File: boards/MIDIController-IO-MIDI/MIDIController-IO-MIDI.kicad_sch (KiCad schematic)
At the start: 44 parts, among them J1 MIDI In 1, J10 MIDICon, J2 MIDI In 2, J3 MIDI In 3, J4 MIDI In 4, J5 MIDI In Pedal, J6 MIDI Out 1, J7 MIDI Out 2, J8 MIDI Out 3, J9 MIDI Out 4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

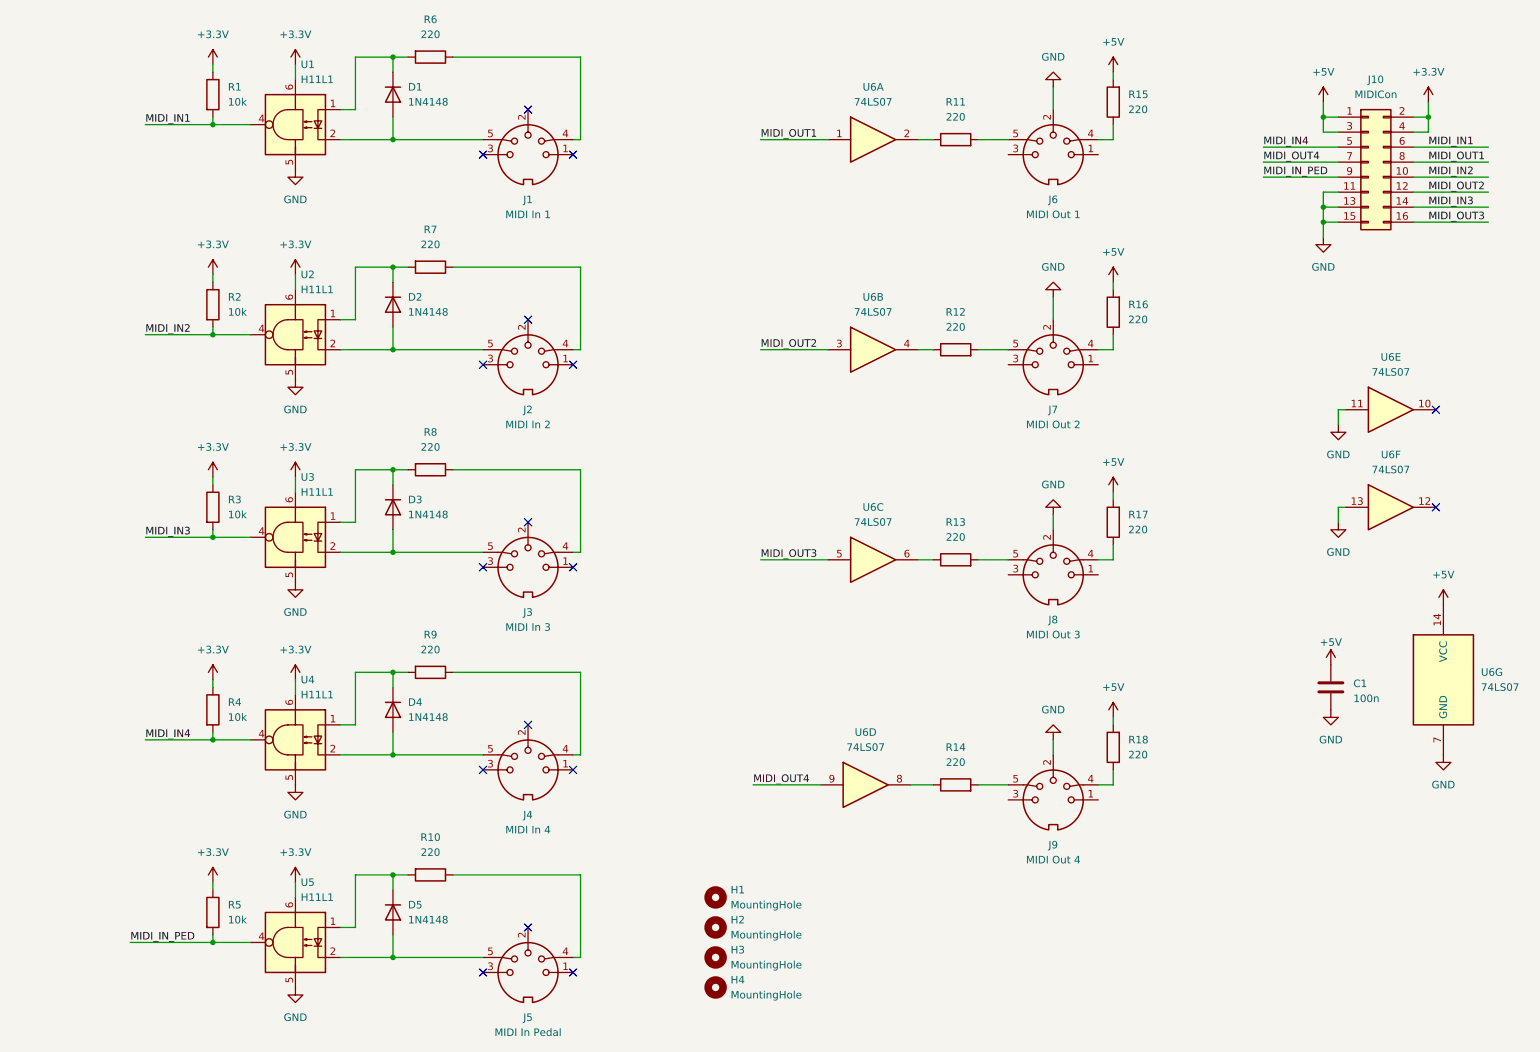
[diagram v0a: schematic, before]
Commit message: Finished PCB for MIDI IO board
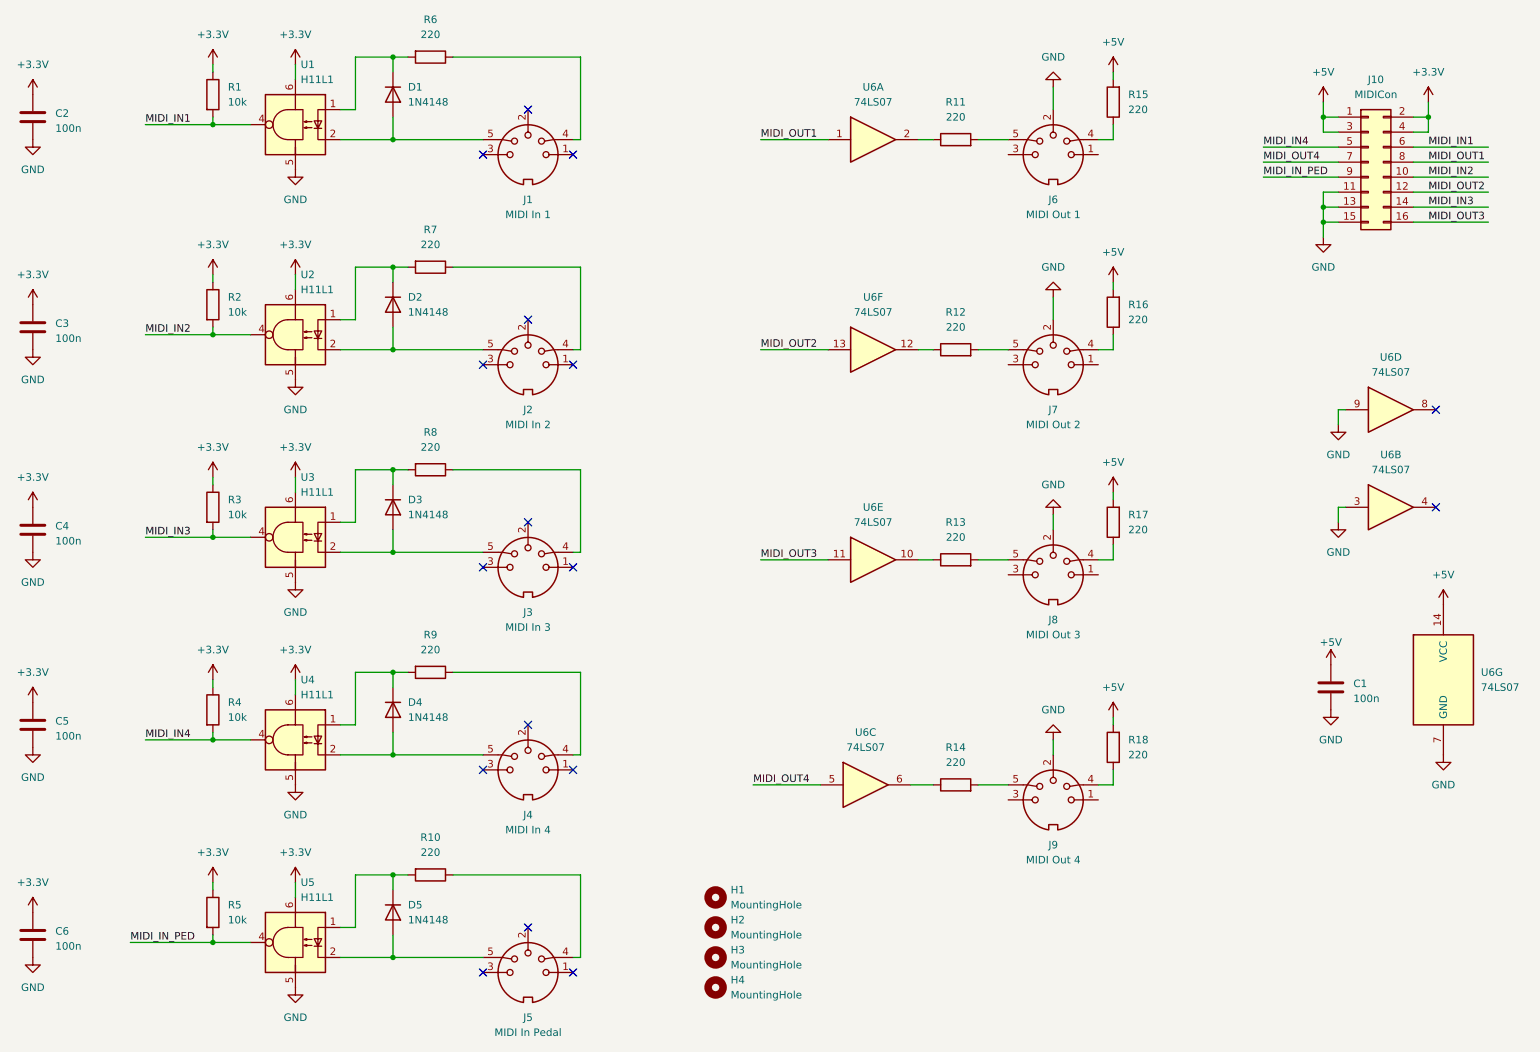
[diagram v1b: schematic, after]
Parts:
- added C2, C3, C4, C5, C6: 100n, Capacitor_THT:C_Disc_D5.0mm_W2.5mm_P5.00mm, symbol Device:C
- R1, R10, R11, R12, R13, R14, R15, R16, R17, R18, R2, R3, R4, R5, R6, R7, R8, R9: footprint Resistor_THT:R_Axial_DIN0204_L3.6mm_D1.6mm_P2.54mm_Vertical -> Resistor_THT:R_Axial_DIN0204_L3.6mm_D1.6mm_P7.62mm_Horizontal
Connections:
- net +3.3V: now also C2.1, C3.1, C4.1, C5.1, C6.1
- net GND: now also U6.3, U6.9, C2.2, C3.2, C4.2, C5.2, C6.2; no longer U6.11, U6.13
- net MIDI_OUT2: now also U6.13; no longer U6.3
- net MIDI_OUT3: now also U6.11; no longer U6.5
- net MIDI_OUT4: now also U6.5; no longer U6.9
- net at R14.1: now also U6.6; no longer U6.8
- net at U6.12: now also R12.1
- net at R13.1: now also U6.10; no longer U6.6
- net at U6.4: no longer R12.1
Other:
- moved on the sheet: U6B, U6C, U6D, U6E, U6F

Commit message: Added Optocoupler and RS232 converter to UART board lines.
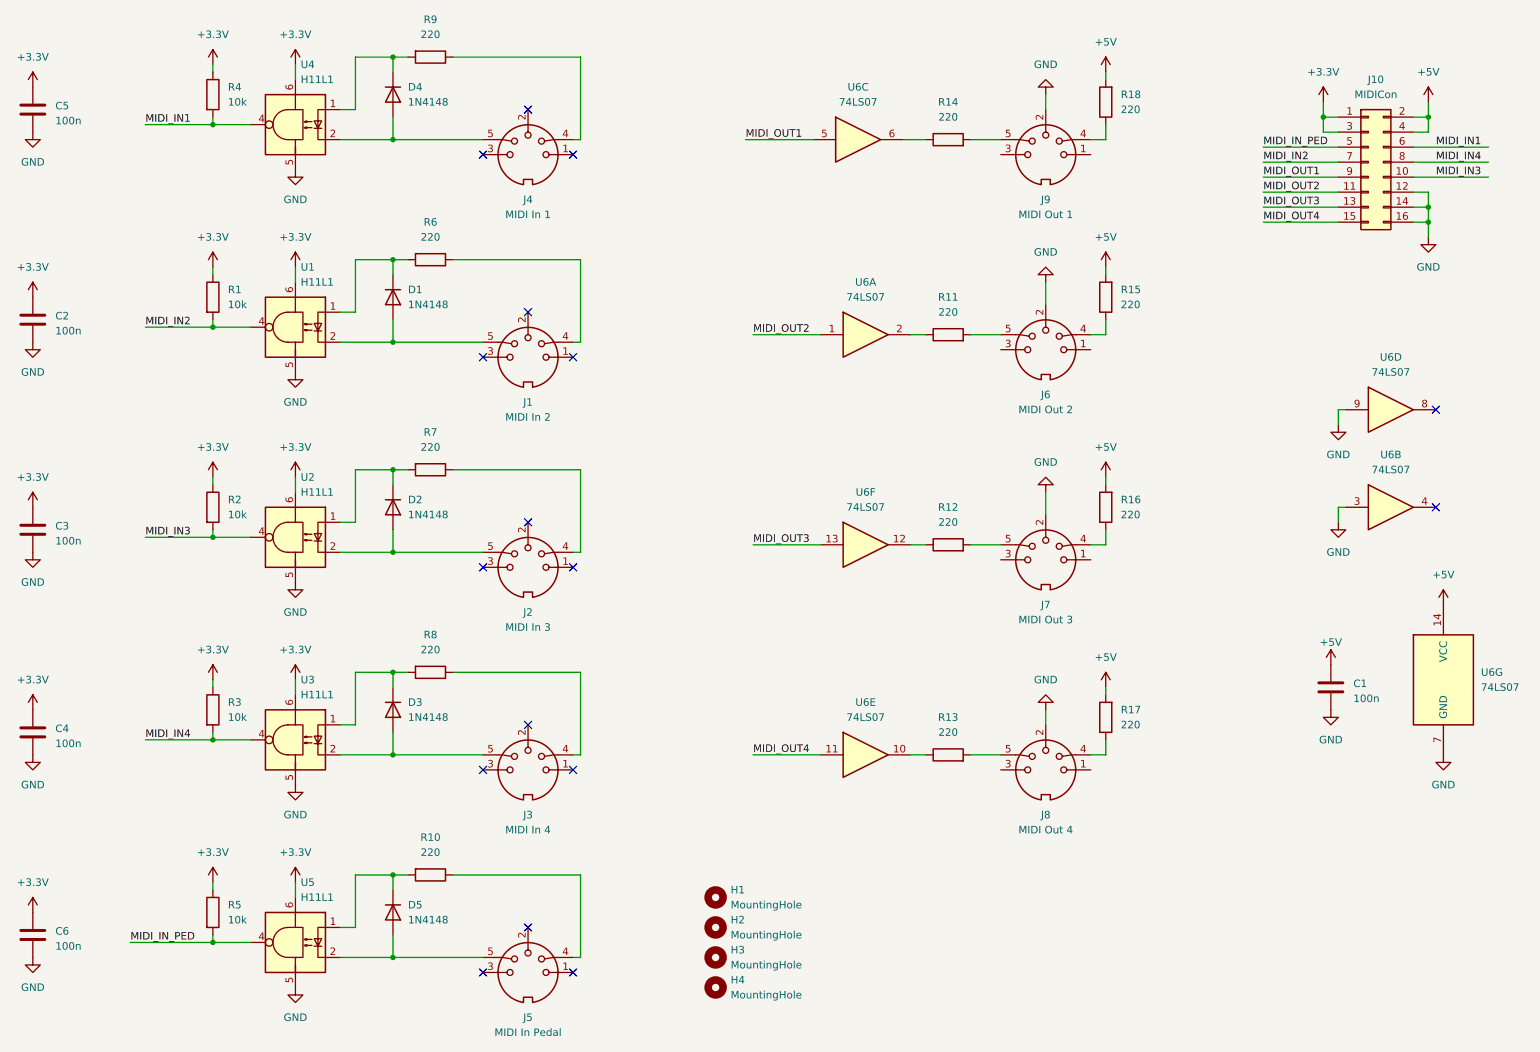
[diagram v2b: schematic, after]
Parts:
- J1: value MIDI In 1 -> MIDI In 2
- J2: value MIDI In 2 -> MIDI In 3
- J3: value MIDI In 3 -> MIDI In 4
- J4: value MIDI In 4 -> MIDI In 1
- J6: value MIDI Out 1 -> MIDI Out 2
- J7: value MIDI Out 2 -> MIDI Out 3
- J8: value MIDI Out 3 -> MIDI Out 4
- J9: value MIDI Out 4 -> MIDI Out 1
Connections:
- net +3.3V: now also J10.1 (Pin_1), J10.3 (Pin_3); no longer J10.2 (Pin_2), J10.4 (Pin_4)
- net +5V: now also J10.2 (Pin_2), J10.4 (Pin_4); no longer J10.1 (Pin_1), J10.3 (Pin_3)
- net GND: now also J10.12 (Pin_12), J10.14 (Pin_14), J10.16 (Pin_16); no longer J10.11 (Pin_11), J10.13 (Pin_13), J10.15 (Pin_15)
- net MIDI_IN1: now also R4.2, U4.4; no longer R1.2, U1.4
- net MIDI_IN2: now also J10.7 (Pin_7), R1.2, U1.4; no longer J10.10 (Pin_10), R2.2, U2.4
- net MIDI_IN3: now also J10.10 (Pin_10), R2.2, U2.4; no longer J10.14 (Pin_14), R3.2, U3.4
- net MIDI_IN4: now also J10.8 (Pin_8), R3.2, U3.4; no longer J10.5 (Pin_5), R4.2, U4.4
- net MIDI_IN_PED: now also J10.5 (Pin_5); no longer J10.9 (Pin_9)
- net MIDI_OUT1: now also J10.9 (Pin_9), U6.5; no longer J10.8 (Pin_8), U6.1
- net MIDI_OUT2: now also J10.11 (Pin_11), U6.1; no longer J10.12 (Pin_12), U6.13
- net MIDI_OUT3: now also J10.13 (Pin_13), U6.13; no longer J10.16 (Pin_16), U6.11
- net MIDI_OUT4: now also J10.15 (Pin_15), U6.11; no longer J10.7 (Pin_7), U6.5
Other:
- moved on the sheet: C2, C3, C4, C5, D1, D2, D3, D4, J1, J2, J3, J4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

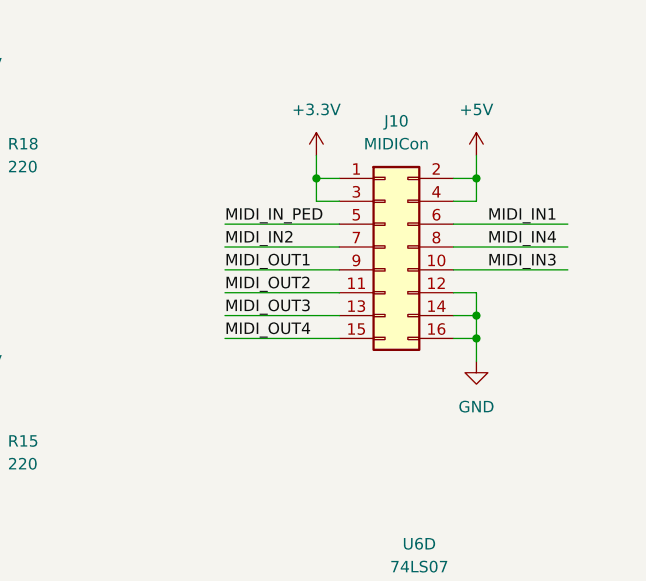
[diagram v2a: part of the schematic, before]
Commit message: Added bypass caps to power supplies, use cheaper MAX232 IC.
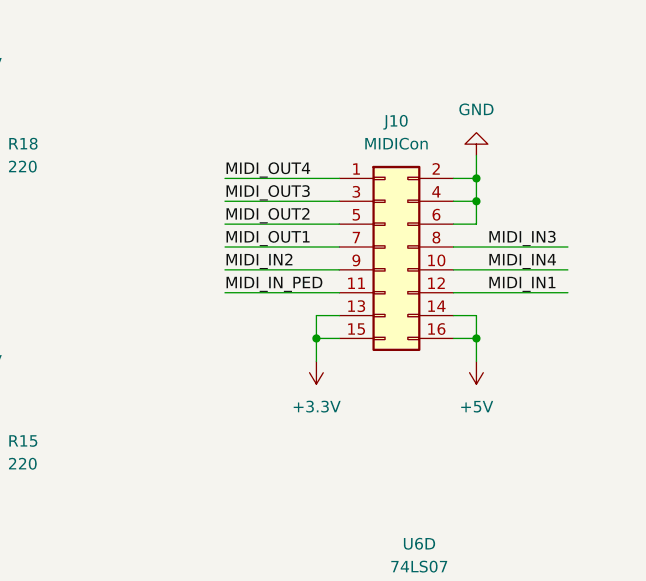
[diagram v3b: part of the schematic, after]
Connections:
- net +3.3V: now also J10.13 (Pin_13), J10.15 (Pin_15); no longer J10.1 (Pin_1), J10.3 (Pin_3)
- net +5V: now also J10.14 (Pin_14), J10.16 (Pin_16); no longer J10.2 (Pin_2), J10.4 (Pin_4)
- net GND: now also J10.2 (Pin_2), J10.4 (Pin_4), J10.6 (Pin_6); no longer J10.12 (Pin_12), J10.14 (Pin_14), J10.16 (Pin_16)
- net MIDI_IN1: now also J10.12 (Pin_12); no longer J10.6 (Pin_6)
- net MIDI_IN2: now also J10.9 (Pin_9); no longer J10.7 (Pin_7)
- net MIDI_IN3: now also J10.8 (Pin_8); no longer J10.10 (Pin_10)
- net MIDI_IN4: now also J10.10 (Pin_10); no longer J10.8 (Pin_8)
- net MIDI_IN_PED: now also J10.11 (Pin_11); no longer J10.5 (Pin_5)
- net MIDI_OUT1: now also J10.7 (Pin_7); no longer J10.9 (Pin_9)
- net MIDI_OUT2: now also J10.5 (Pin_5); no longer J10.11 (Pin_11)
- net MIDI_OUT3: now also J10.3 (Pin_3); no longer J10.13 (Pin_13)
- net MIDI_OUT4: now also J10.1 (Pin_1); no longer J10.15 (Pin_15)
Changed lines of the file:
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@@
 	)
 	(junction
-		(at 260.35 52.07)
+		(at 260.35 39.37)
 		(diameter 0)
 		(color 0 0 0 0)
 	)
 	(junction
-		(at 242.57 36.83)
+		(at 242.57 54.61)
 		(diameter 0)
 		(color 0 0 0 0)
@@
 	)
 	(junction
-		(at 260.35 36.83)
+		(at 260.35 54.61)
 		(diameter 0)
 		(color 0 0 0 0)
@@
 	)
 	(junction
-		(at 260.35 54.61)
+		(at 260.35 36.83)
 		(diameter 0)
 		(color 0 0 0 0)
@@
 	(wire
 		(pts
-			(xy 257.81 52.07) (xy 260.35 52.07)
+			(xy 257.81 39.37) (xy 260.35 39.37)
 		)
 		(stroke
@@
 	(wire
 		(pts
-			(xy 242.57 36.83) (xy 242.57 39.37)
+			(xy 242.57 54.61) (xy 242.57 52.07)
 		)
 		(stroke
@@
 	(wire
 		(pts
-			(xy 232.41 44.45) (xy 245.11 44.45)
+			(xy 232.41 46.99) (xy 245.11 46.99)
 		)
 		(stroke
@@
 	(wire
 		(pts
-			(xy 232.41 49.53) (xy 245.11 49.53)
+			(xy 232.41 41.91) (xy 245.11 41.91)
 		)
 		(stroke
@@
 	(wire
 		(pts
-			(xy 242.57 39.37) (xy 245.11 39.37)
+			(xy 242.57 52.07) (xy 245.11 52.07)
 		)
 		(stroke
@@
 	(wire
 		(pts
-			(xy 232.41 41.91) (xy 245.11 41.91)
+			(xy 232.41 49.53) (xy 245.11 49.53)
 		)
 		(stroke
@@
 	(wire
 		(pts
-			(xy 260.35 54.61) (xy 260.35 57.15)
+			(xy 260.35 36.83) (xy 260.35 34.29)
 		)
 		(stroke
@@
 	(wire
 		(pts
-			(xy 232.41 54.61) (xy 245.11 54.61)
+			(xy 232.41 36.83) (xy 245.11 36.83)
 		)
 		(stroke
@@
 	(wire
 		(pts
-			(xy 257.81 39.37) (xy 260.35 39.37)
+			(xy 257.81 52.07) (xy 260.35 52.07)
 		)
 		(stroke
@@
 	(wire
 		(pts
-			(xy 232.41 46.99) (xy 245.11 46.99)
+			(xy 232.41 44.45) (xy 245.11 44.45)
 		)
 		(stroke
@@
 	(wire
 		(pts
-			(xy 260.35 36.83) (xy 260.35 34.29)
+			(xy 260.35 54.61) (xy 260.35 57.15)
 		)
 		(stroke
@@
 	(wire
 		(pts
-			(xy 260.35 39.37) (xy 260.35 36.83)
+			(xy 260.35 52.07) (xy 260.35 54.61)
 		)
 		(stroke
@@
 	(wire
 		(pts
-			(xy 232.41 52.07) (xy 245.11 52.07)
+			(xy 232.41 39.37) (xy 245.11 39.37)
 		)
 		(stroke
@@
 	(wire
 		(pts
-			(xy 260.35 52.07) (xy 260.35 54.61)
+			(xy 260.35 39.37) (xy 260.35 36.83)
 		)
 		(stroke
@@
 	(wire
 		(pts
-			(xy 260.35 49.53) (xy 260.35 52.07)
+			(xy 260.35 41.91) (xy 260.35 39.37)
 		)
 		(stroke
@@
 	(wire
 		(pts
-			(xy 242.57 34.29) (xy 242.57 36.83)
+			(xy 242.57 57.15) (xy 242.57 54.61)
 		)
 		(stroke
@@
 	(wire
 		(pts
-			(xy 257.81 41.91) (xy 270.51 41.91)
+			(xy 257.81 49.53) (xy 270.51 49.53)
 		)
 		(stroke
@@
 	(wire
 		(pts
-			(xy 257.81 46.99) (xy 270.51 46.99)
+			(xy 257.81 44.45) (xy 270.51 44.45)
 		)
 		(stroke
@@
 	(wire
 		(pts
-			(xy 242.57 36.83) (xy 245.11 36.83)
+			(xy 242.57 54.61) (xy 245.11 54.61)
 		)
 		(stroke
@@
 	(wire
 		(pts
-			(xy 257.81 54.61) (xy 260.35 54.61)
+			(xy 257.81 36.83) (xy 260.35 36.83)
 		)
 		(stroke
@@
 	(wire
 		(pts
-			(xy 257.81 44.45) (xy 270.51 44.45)
+			(xy 257.81 46.99) (xy 270.51 46.99)
 		)
 		(stroke
@@
 	(wire
 		(pts
-			(xy 257.81 36.83) (xy 260.35 36.83)
+			(xy 257.81 54.61) (xy 260.35 54.61)
 		)
 		(stroke
@@
 	(wire
 		(pts
-			(xy 257.81 49.53) (xy 260.35 49.53)
+			(xy 257.81 41.91) (xy 260.35 41.91)
 		)
 		(stroke
@@
 	)
 	(label "MIDI_OUT1"
-		(at 232.41 46.99 0)
+		(at 232.41 44.45 0)
 		(fields_autoplaced yes)
 		(effects
@@
 	)
 	(label "MIDI_OUT2"
-		(at 232.41 49.53 0)
+		(at 232.41 41.91 0)
 		(fields_autoplaced yes)
 		(effects
@@
 	)
 	(label "MIDI_OUT3"
-		(at 232.41 52.07 0)
+		(at 232.41 39.37 0)
 		(fields_autoplaced yes)
 		(effects
@@
 	)
 	(label "MIDI_IN4"
-		(at 261.62 44.45 0)
+		(at 261.62 46.99 0)
 		(fields_autoplaced yes)
 		(effects
@@
 	)
 	(label "MIDI_IN3"
-		(at 261.62 46.99 0)
+		(at 261.62 44.45 0)
 		(fields_autoplaced yes)
 		(effects
@@
 	)
 	(label "MIDI_IN1"
-		(at 261.62 41.91 0)
+		(at 261.62 49.53 0)
 		(fields_autoplaced yes)
 		(effects
@@
 	)
 	(label "MIDI_OUT4"
-		(at 232.41 54.61 0)
+		(at 232.41 36.83 0)
 		(fields_autoplaced yes)
 		(effects
@@
 	)
 	(label "MIDI_IN_PED"
-		(at 232.41 41.91 0)
+		(at 232.41 49.53 0)
 		(fields_autoplaced yes)
 		(effects
@@
 	)
 	(label "MIDI_IN2"
-		(at 232.41 44.45 0)
+		(at 232.41 46.99 0)
 		(fields_autoplaced yes)
 		(effects
@@
 	(symbol
 		(lib_id "power:+5V")
-		(at 260.35 34.29 0)
+		(at 260.35 57.15 0)
+		(mirror x)
 		(unit 1)
 		(exclude_from_sim no)
@@
 		(fields_autoplaced yes)
 		(property "Reference" "#PWR030"
-			(at 260.35 38.1 0)
+			(at 260.35 53.34 0)
 			(effects
 				(font
@@
 		)
 		(property "Value" "+5V"
-			(at 260.35 29.21 0)
+			(at 260.35 62.23 0)
 			(effects
 				(font
@@
 		)
 		(property "Footprint" ""
-			(at 260.35 34.29 0)
+			(at 260.35 57.15 0)
 			(effects
 				(font
@@
 		)
 		(property "Datasheet" ""
-			(at 260.35 34.29 0)
+			(at 260.35 57.15 0)
 			(effects
 				(font
@@
 		)
 		(property "Description" "Power symbol creates a global label with name \"+5V\""
-			(at 260.35 34.29 0)
+			(at 260.35 57.15 0)
 			(effects
 				(font
@@
 		(on_board yes)
 		(dnp no)
-		(fields_autoplaced yes)
 		(property "Reference" "J10"
 			(at 251.46 30.48 0)
@@
 	(symbol
 		(lib_id "power:GND")
-		(at 260.35 57.15 0)
+		(at 260.35 34.29 0)
+		(mirror x)
 		(unit 1)
 		(exclude_from_sim no)
@@
 		(fields_autoplaced yes)
 		(property "Reference" "#PWR032"
-			(at 260.35 63.5 0)
+			(at 260.35 27.94 0)
 			(effects
 				(font
@@
 		)
 		(property "Value" "GND"
-			(at 260.35 62.23 0)
+			(at 260.35 29.21 0)
 			(effects
 				(font
@@
 		)
 		(property "Footprint" ""
-			(at 260.35 57.15 0)
+			(at 260.35 34.29 0)
 			(effects
 				(font
@@
 		)
 		(property "Datasheet" ""
-			(at 260.35 57.15 0)
+			(at 260.35 34.29 0)
 			(effects
 				(font
@@
 		)
 		(property "Description" "Power symbol creates a global label with name \"GND\" , ground"
-			(at 260.35 57.15 0)
+			(at 260.35 34.29 0)
 			(effects
 				(font
@@
 	(symbol
 		(lib_id "power:+3.3V")
-		(at 242.57 34.29 0)
+		(at 242.57 57.15 0)
+		(mirror x)
 		(unit 1)
 		(exclude_from_sim no)
@@
 		(fields_autoplaced yes)
 		(property "Reference" "#PWR031"
-			(at 242.57 38.1 0)
+			(at 242.57 53.34 0)
 			(effects
 				(font
@@
 		)
 		(property "Value" "+3.3V"
-			(at 242.57 29.21 0)
+			(at 242.57 62.23 0)
 			(effects
 				(font
@@
 		)
 		(property "Footprint" ""
-			(at 242.57 34.29 0)
+			(at 242.57 57.15 0)
 			(effects
 				(font
@@
 		)
 		(property "Datasheet" ""
-			(at 242.57 34.29 0)
+			(at 242.57 57.15 0)
 			(effects
 				(font
@@
 		)
 		(property "Description" "Power symbol creates a global label with name \"+3.3V\""
-			(at 242.57 34.29 0)
+			(at 242.57 57.15 0)
 			(effects
 				(font
